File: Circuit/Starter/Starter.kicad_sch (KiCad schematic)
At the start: 13 parts

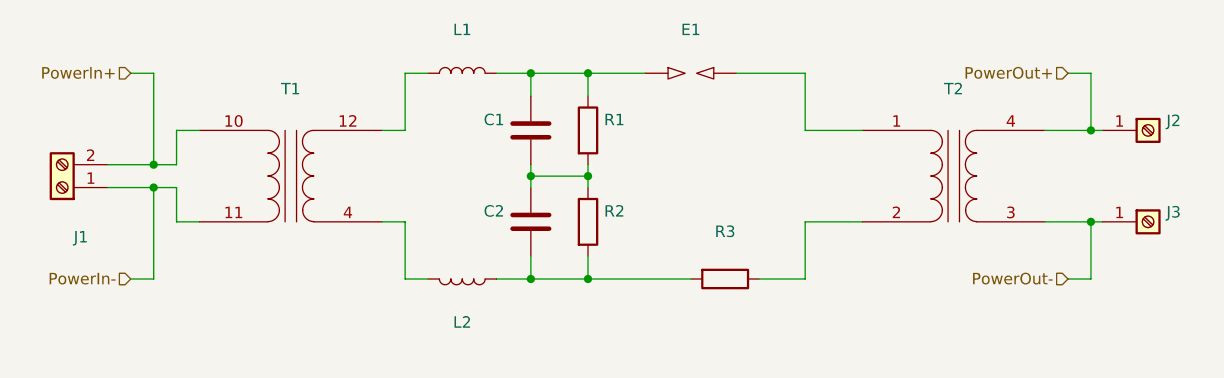
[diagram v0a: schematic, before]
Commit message: [Circuit] Start designing a solid state starter based on class-E Tesla coil
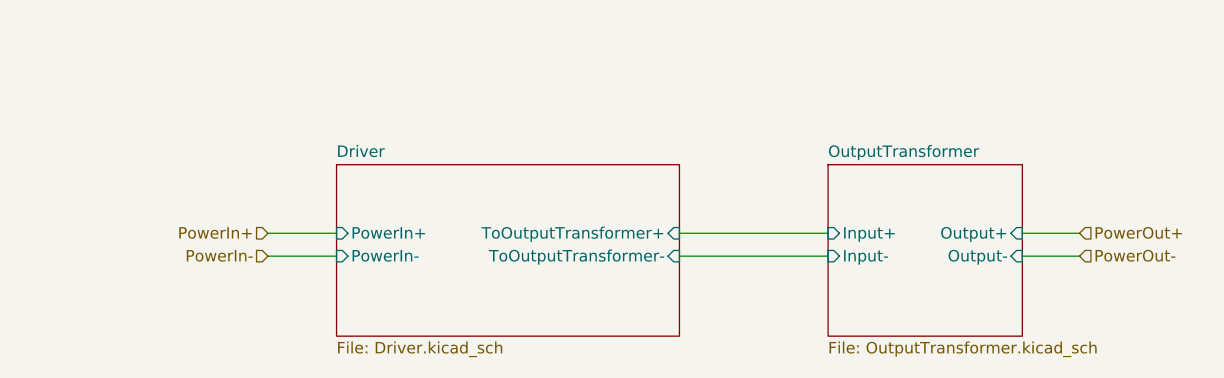
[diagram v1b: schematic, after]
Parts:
- removed C1, C2: (no value), symbol Device:C
- removed E1: (no value), symbol Starter-rescue:SPARK_GAP-Device
- removed J1: (no value), symbol Connector:Screw_Terminal_01x02
- removed J2, J3: (no value), symbol Connector:Screw_Terminal_01x01
- removed L1, L2: (no value), symbol Device:L
- removed R1, R2, R3: (no value), symbol Device:R
- removed T1: (no value), symbol CustomizedFlybackTransformer:FlybackTransformer
- removed T2: (no value), symbol Device:Transformer_1P_1S
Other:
- added sheet Driver (Driver.kicad_sch)
- added sheet OutputTransformer (OutputTransformer.kicad_sch)
- title: Starter Module -> Starter Subsystem
